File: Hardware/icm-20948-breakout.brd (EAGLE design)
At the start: 19.3 x 10.5 mm, 11 parts, among them J1 455-1750-1-ND, J2 455-1750-1-ND, U1 NCP563, U2 NTS0104, U3 ICM-20948

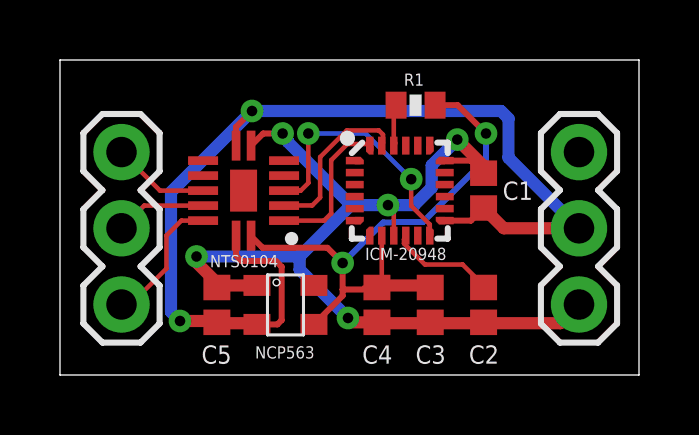
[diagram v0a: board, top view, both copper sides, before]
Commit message: Connected unused io pins on the level translator to ground.
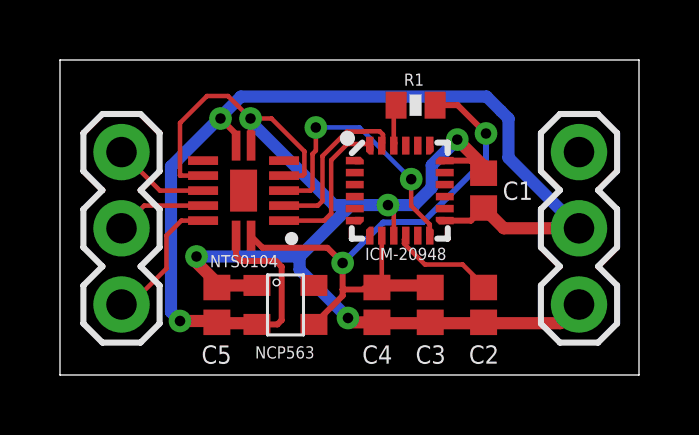
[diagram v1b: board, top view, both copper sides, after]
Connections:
- net GND: now also U2.10, U2.5
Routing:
- net GND: track 33.0 -> 43.2 mm
- net VCC: track 35.6 -> 36.3 mm
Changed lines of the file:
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@@
 <drawing>
 <settings>
-<setting alwaysvectorfont="no"/>
+<setting alwaysvectorfont="yes"/>
 <setting verticaltext="up"/>
 </settings>
@@
 <wire x1="10.9069" y1="5.638" x2="10.9323" y2="5.6634" width="0.4064" layer="16"/>
 <via x="13.243" y="7.847" extent="1-16" drill="0.35"/>
-<wire x1="7.45" y1="7.95" x2="7.42" y2="7.98" width="0.2" layer="16"/>
-<wire x1="7.42" y1="7.98" x2="7.42" y2="8.05" width="0.2" layer="16"/>
-<via x="7.42" y="8.05" extent="1-16" drill="0.35"/>
-<wire x1="7.42" y1="8.05" x2="6.773" y2="8.05" width="0.2" layer="1"/>
-<wire x1="6.773" y1="8.05" x2="6.369" y2="7.646" width="0.2" layer="1"/>
 <wire x1="14.12" y1="6.726" x2="14.12" y2="6.97" width="0.4064" layer="1"/>
 <wire x1="14.12" y1="6.97" x2="13.243" y2="7.847" width="0.4064" layer="1"/>
@@
 <wire x1="17.3" y1="2.35" x2="16.6764" y2="1.7264" width="0.4064" layer="1"/>
 <wire x1="16.6764" y1="1.7264" x2="14.12" y2="1.7264" width="0.4064" layer="1"/>
-<wire x1="7.595" y1="7.7680875" x2="7.595" y2="7.805" width="0.4064" layer="16"/>
-<wire x1="7.595" y1="7.805" x2="7.42" y2="7.98" width="0.4064" layer="16"/>
 <wire x1="10.9323" y1="5.6634" x2="9.6996875" y2="5.6634" width="0.4064" layer="16"/>
-<wire x1="9.6996875" y1="5.6634" x2="7.595" y2="7.7680875" width="0.4064" layer="16"/>
 <wire x1="9.6996875" y1="5.6634" x2="7.9862875" y2="3.95" width="0.4064" layer="16"/>
 <via x="4.55" y="3.95" extent="1-16" drill="0.35"/>
@@
 <wire x1="9.6" y1="1.9" x2="7.9862875" y2="3.5137125" width="0.4064" layer="16"/>
 <wire x1="7.9862875" y1="3.5137125" x2="7.9862875" y2="3.95" width="0.4064" layer="16"/>
+<wire x1="9.6996875" y1="5.6634" x2="9.1366" y2="5.6634" width="0.4064" layer="16"/>
+<wire x1="9.1366" y1="5.6634" x2="6.35" y2="8.45" width="0.4064" layer="16"/>
+<wire x1="6.35" y1="8.45" x2="6.35" y2="8.55" width="0.2" layer="16"/>
+<via x="6.35" y="8.55" extent="1-16" drill="0.35"/>
+<wire x1="6.35" y1="8.55" x2="6.35" y2="7.665" width="0.2" layer="1"/>
+<wire x1="6.35" y1="7.665" x2="6.369" y2="7.646" width="0.2" layer="1"/>
+<contactref element="U2" pad="5"/>
+<contactref element="U2" pad="10"/>
+<wire x1="7.469" y1="6.646" x2="8.096" y2="6.646" width="0.1524" layer="1"/>
+<wire x1="8.1468" y1="6.6968" x2="8.1468" y2="7.4532" width="0.1524" layer="1"/>
+<wire x1="8.096" y1="6.646" x2="8.1468" y2="6.6968" width="0.1524" layer="1"/>
+<wire x1="7.05" y1="8.55" x2="6.35" y2="8.55" width="0.1524" layer="1"/>
+<wire x1="8.1468" y1="7.4532" x2="7.05" y2="8.55" width="0.1524" layer="1"/>
+<wire x1="4.769" y1="6.646" x2="4.004" y2="6.646" width="0.1524" layer="1"/>
+<wire x1="4.004" y1="6.646" x2="4" y2="6.65" width="0.1524" layer="1"/>
+<wire x1="4" y1="8.4" x2="4.9" y2="9.3" width="0.1524" layer="1"/>
+<wire x1="4.9" y1="9.3" x2="5.6" y2="9.3" width="0.1524" layer="1"/>
+<wire x1="5.6" y1="9.3" x2="6.35" y2="8.55" width="0.1524" layer="1"/>
+<wire x1="4" y1="6.65" x2="4" y2="8.4" width="0.1524" layer="1"/>
 </signal>
 <signal name="VCC">
@@
 <wire x1="5.869" y1="3.981" x2="5.869" y2="4.646" width="0.2" layer="1"/>
 <wire x1="7.247" y1="1.686" x2="7.389" y2="1.828" width="0.2" layer="1"/>
-<wire x1="5.869" y1="8.269" x2="5.869" y2="7.646" width="0.2" layer="1"/>
 <wire x1="14.95" y1="8.55" x2="14.7" y2="8.8" width="0.4064" layer="16"/>
-<wire x1="14.7" y1="8.8" x2="6.45" y2="8.8" width="0.4064" layer="16"/>
-<wire x1="6.45" y1="8.8" x2="6.4" y2="8.8" width="0.2" layer="16"/>
-<via x="6.4" y="8.8" extent="1-16" drill="0.35"/>
-<wire x1="6.4" y1="8.8" x2="5.869" y2="8.269" width="0.2" layer="1"/>
 <contactref element="J2" pad="2"/>
 <wire x1="17.3" y1="4.89" x2="14.796" y2="4.89" width="0.4064" layer="1"/>
@@
 <wire x1="17.3" y1="4.89" x2="14.95" y2="7.24" width="0.4064" layer="16"/>
 <wire x1="14.95" y1="7.24" x2="14.95" y2="8.55" width="0.4064" layer="16"/>
-<wire x1="6.4" y1="8.8" x2="3.7" y2="6.1" width="0.4064" layer="16"/>
-<wire x1="3.7" y1="2.1" x2="4" y2="1.8" width="0.4064" layer="16"/>
+<wire x1="4" y1="1.8" x2="3.7" y2="2.1" width="0.4064" layer="16"/>
 <via x="4" y="1.8" extent="1-16" drill="0.35"/>
 <wire x1="4" y1="1.8" x2="5.2453" y2="1.8" width="0.4064" layer="1"/>
 <wire x1="5.2453" y1="1.8" x2="5.3189" y2="1.7264" width="0.4064" layer="1"/>
-<wire x1="3.7" y1="6.1" x2="3.7" y2="2.1" width="0.4064" layer="16"/>
+<wire x1="5.3" y1="8.55" x2="5.35" y2="8.55" width="0.4064" layer="16"/>
+<via x="5.35" y="8.55" extent="1-16" drill="0.35"/>
+<wire x1="5.35" y1="8.55" x2="5.869" y2="8.031" width="0.2" layer="1"/>
+<wire x1="5.869" y1="8.031" x2="5.869" y2="7.646" width="0.2" layer="1"/>
+<wire x1="3.7" y1="2.1" x2="3.7" y2="6.95" width="0.4064" layer="16"/>
+<wire x1="3.7" y1="6.95" x2="5.3" y2="8.55" width="0.4064" layer="16"/>
+<wire x1="14.7" y1="8.8" x2="14.2192" y2="9.2808" width="0.4064" layer="16"/>
+<wire x1="6.0308" y1="9.2808" x2="5.3" y2="8.55" width="0.4064" layer="16"/>
+<wire x1="14.2192" y1="9.2808" x2="6.0308" y2="9.2808" width="0.4064" layer="16"/>
 </signal>
 <signal name="N$1">
@@
 <contactref element="U2" pad="3"/>
 <wire x1="10.7672" y1="8.0129" x2="10.7672" y2="7.7335" width="0.1524" layer="1"/>
-<wire x1="10.6275" y1="8.1526" x2="10.7672" y2="8.0129" width="0.1524" layer="1"/>
-<wire x1="9.5607" y1="8.1526" x2="10.6275" y2="8.1526" width="0.1524" layer="1"/>
-<wire x1="8.6717" y1="7.2636" x2="9.5607" y2="8.1526" width="0.1524" layer="1"/>
-<wire x1="8.6717" y1="5.9174" x2="8.6717" y2="7.2636" width="0.1524" layer="1"/>
-<wire x1="8.405" y1="5.6507" x2="8.6717" y2="5.9174" width="0.1524" layer="1"/>
-<wire x1="7.473396875" y1="5.6507" x2="8.405" y2="5.6507" width="0.1524" layer="1"/>
 <wire x1="10.7672" y1="7.7335" x2="10.726" y2="7.646" width="0.1524" layer="1"/>
 <wire x1="7.473396875" y1="5.6507" x2="7.469" y2="5.646" width="0.1524" layer="1"/>
+<wire x1="7.469" y1="5.646" x2="8.596" y2="5.646" width="0.1524" layer="1"/>
+<wire x1="8.75" y1="5.8" x2="8.75" y2="7.3" width="0.1524" layer="1"/>
+<wire x1="8.75" y1="7.3" x2="9.5607" y2="8.1107" width="0.1524" layer="1"/>
+<wire x1="8.596" y1="5.646" x2="8.75" y2="5.8" width="0.1524" layer="1"/>
+<wire x1="9.5607" y1="8.1107" x2="10.11425" y2="8.1107" width="0.1524" layer="1"/>
+<wire x1="10.11425" y1="8.1107" x2="10.12735" y2="8.1238" width="0.1524" layer="1"/>
+<wire x1="10.12735" y1="8.1238" x2="10.6563" y2="8.1238" width="0.1524" layer="1"/>
+<wire x1="10.6563" y1="8.1238" x2="10.7672" y2="8.0129" width="0.1524" layer="1"/>
 </signal>
 <signal name="INT3-1_8">
@@
 <wire x1="11.707" y1="5.638" x2="11.707" y2="6.527" width="0.1524" layer="1"/>
 <via x="11.707" y="6.527" extent="1-16" drill="0.35"/>
-<wire x1="11.707" y1="6.527" x2="10.183" y2="8.051" width="0.1524" layer="16"/>
-<wire x1="10.183" y1="8.051" x2="8.278" y2="8.051" width="0.1524" layer="16"/>
-<via x="8.278" y="8.051" extent="1-16" drill="0.35"/>
-<wire x1="8.278" y1="8.051" x2="8.278" y2="6.4" width="0.1524" layer="1"/>
-<wire x1="8.278" y1="6.4" x2="8.024" y2="6.146" width="0.1524" layer="1"/>
-<wire x1="8.024" y1="6.146" x2="7.469" y2="6.146" width="0.1524" layer="1"/>
+<via x="8.528" y="8.251" extent="1-16" drill="0.35"/>
 <wire x1="12.326" y1="5.019" x2="11.707" y2="5.638" width="0.1524" layer="1"/>
+<wire x1="7.469" y1="6.146" x2="8.346" y2="6.146" width="0.1524" layer="1"/>
+<wire x1="8.4177" y1="6.2177" x2="8.4177" y2="7.3688125" width="0.1524" layer="1"/>
+<wire x1="8.4177" y1="7.3688125" x2="8.528" y2="7.4791125" width="0.1524" layer="1"/>
+<wire x1="8.528" y1="7.4791125" x2="8.528" y2="8.251" width="0.1524" layer="1"/>
+<wire x1="8.346" y1="6.146" x2="8.4177" y2="6.2177" width="0.1524" layer="1"/>
+<wire x1="8.528" y1="8.251" x2="9.983" y2="8.251" width="0.1524" layer="16"/>
+<wire x1="9.983" y1="8.251" x2="11.707" y2="6.527" width="0.1524" layer="16"/>
 </signal>
 <signal name="SCL3">

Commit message: Redesign after comments. Changed footprints of capacitors. Removed routing under ICS. Connected nCS to level switcher to avoid a resistor. Added solder jumper to set address. Added ground planes on both sides.
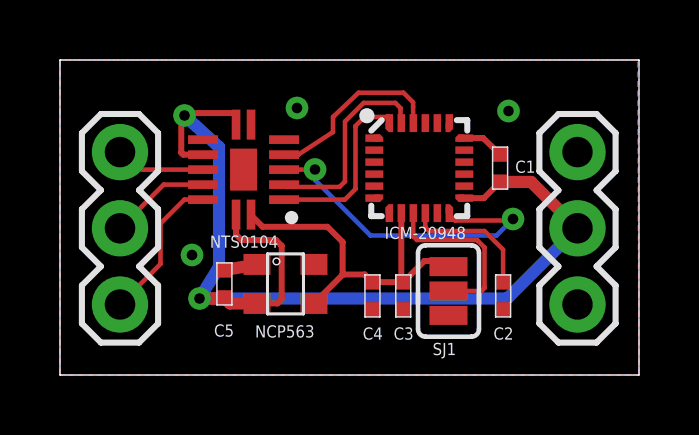
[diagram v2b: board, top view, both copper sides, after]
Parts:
- removed R1: 10k, SparkFun-Passives:0402-RES
- added SJ1: JUMPER-32-3, SparkFun-Passives:SJ_3_PASTE2&3
- C1, C2, C3, C4, C5: device SparkFun-Capacitors:0402 -> FaBo-Capacitor:0402
- moved U3 0.99 mm to (12.0, 6.90)
- moved C3 0.95 mm to (11.4, 2.64)
- moved C1 0.93 mm to (14.7, 6.90)
- moved C5 0.74 mm to (5.48, 3.04)
- moved C2 0.72 mm to (14.8, 2.64)
- moved U1 0.70 mm to (7.52, 3.04)
- moved U2 0.70 mm to (6.12, 6.85)
- moved C4 0.34 mm to (10.4, 2.64)
- moved J2 0.05 mm to (17.2, 2.35)
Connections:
- removed net N$4: R1.1, U3.22
- new net CS-1_8: U2.5, U3.22
- new net N$2: SJ1.2, U3.9
- net GND: now also C1.P$2, C2.P$2, C3.P$2, C4.P$2, C5.P$2, SJ1.3; no longer C1.2, C2.2, C3.2, C4.2, C5.2, U2.10, U2.5, U3.9
- net N$1: now also C2.P$1; no longer C2.1
- net VCC: now also C1.P$1, C5.P$1, U2.10; no longer C1.1, C5.1
- net VDD1_8: now also C3.P$1, C4.P$1, SJ1.1; no longer C3.1, C4.1, R1.2
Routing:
- net GND: track 43.2 -> 2.69 mm, vias 5 -> 3
- net VDD1_8: track 20.3 -> 12.4 mm, vias 2 -> 0
- net CS-1_8: track 0.00 -> 6.21 mm
- net N$2: track 0.00 -> 5.89 mm
- net INT3-1_8: track 9.14 -> 11.4 mm
- net N$4: track 1.49 -> 0.00 mm
- net SCL3-1_8: track 5.63 -> 6.82 mm
- net SDA3-1_8: track 4.96 -> 6.03 mm
- net N$1: track 3.58 -> 4.52 mm
- added copper zone on layer 1, net GND
- added copper zone on layer 16, net GND
